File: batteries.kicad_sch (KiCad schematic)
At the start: 29 parts, among them IC1 BQ7791501PWR, Q8 BSZ067N06LS3_G, Q9 BSZ067N06LS3_G

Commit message: Test commit
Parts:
- removed D2, D3, D4: CUS10S30, 30V 1A, CUS357H3F, symbol HEDGE2:CUS10S30
- added C76, C88: 1u, symbol Device:C_Small
- added C77, C78: 10u, symbol Device:C_Small
- added C79, C80, C81, C82, C83, C84, C85, C86, C87: 100n, symbol Device:C_Small
- added D15, D16, D2, D3, D5: CDBA240LL-HF, 40V 2A, DIOM5225X250N, symbol HEDGE2:CDBA240LL-HF
- added D17, D18, D19: LED, symbol Device:LED
- added IC23: BQ24610RGER, QFN50P400X400X100-25N-D, symbol HEDGE2:BQ24610RGER
- added L2: ETQP4M6R8KVK - 6u8, ETQ-P4M_KVK, symbol HEDGE2:ETQP4M6R8KVK
- added Q1, Q3: SI7617DN-T1-GE3, SIS862DNT1GE3, symbol HEDGE2:SI7617DN-T1-GE3
- added R55: 10, symbol Device:R_Small
- added R56: 1k, symbol Device:R_Small
- added R57, R58: 1M, symbol Device:R_Small
- added R59, R60, R61: 100k, symbol Device:R_Small
- added R62: 32k4, symbol Device:R_Small
- added R63, R64, R65, R66: 10k, symbol Device:R_Small
- added R67: 9k31, symbol Device:R_Small
- added R68: 430k, symbol Device:R_Small
- added RSR1: 10m, symbol Device:R_Small
- added TH2: 10k, symbol Device:Thermistor_US
- IC1: value BQ7791501PWR -> BQ7791514PWR
- R7: value 1m -> 10m
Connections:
- net +BATT: now also C76.2, C77.2, C78.2, C80.1, C81.2, C82.2, C83.2, C84.1, C84.2, C85.1, C85.2, C86.1, C87.2, C88.2, IC23.13 (SRN), IC23.17 (GND), IC23.25 (EP), Q1.1 (S_1), Q1.2 (S_2), Q1.3 (S_3), R57.2, R58.1, R62.1, R63.1, R68.1, RSR1.2, TH2.1
- net at Q9.1 (S_1), Q9.2 (S_2), Q9.3 (S_3)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: now also D3.2 (A)
- net at R10.1, R11.2: now also D2.2 (A)
- net at IC1.11 (SRN), Q8.1 (S_1), Q8.2 (S_2)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: now also D5.2 (A)
- net at Q8.5 (D_1), Q8.6 (D_2), Q8.7 (D_3)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: now also D3.1 (K), D5.1 (K)
- net at Q9.4 (G), R11.1, R12.2: now also D2.1 (K)
- new net: IC23.11 (ISET1), R61.1, R63.2
- new net: C77.1, C78.1, D16.1 (K), IC23.1 (ACN), IC23.2 (ACP), Q3.5 (D_1), Q3.6 (D_2), Q3.7 (D_3), Q3.8 (D_4), R55.2
- new net: D19.2 (A), R66.2
- new net: C76.1, IC23.24 (VCC), R55.1
- new net: IC23.15 (ISET2), R60.1, R62.2
- new net: C79.2, IC23.20 (PH), L2.1, Q1.5 (D_1), Q1.6 (D_2), Q1.7 (D_3), Q1.8 (D_4), Q3.1 (S_1), Q3.2 (S_2), Q3.3 (S_3)
- new net: IC23.21 (HIDRV), Q3.4 (G)
- new net: D17.2 (A), R64.2
- new net: C80.2, D15.2 (A), IC23.18 (REGN)
- new net: IC23.19 (LODRV), Q1.4 (G)
- new net: D15.1 (K), IC23.22 (BTST), R56.1
- new net: D17.1 (K), IC23.5 (STAT1)
- new net: IC23.6 (TS), R67.1, R68.2, TH2.2
- new net: C81.1, IC23.7 (TTC)
- new net: D19.1 (K), IC23.8 (~{PG})
- new net: D18.1 (K), IC23.9 (STAT2)
- new net: D18.2 (A), R65.2
- new net: C79.1, R56.2
- new net: C87.1, R59.1
- new net +ADAPTER: D16.2 (A), R59.2
- new net SRP: C82.1, C83.1, IC23.14 (SRP), L2.2, RSR1.1
- new net VFB: C86.2, IC23.12 (VFB), R57.1, R58.2
- new net VREF: C88.1, IC23.10 (VREF), IC23.16 (ACSET), IC23.4 (CE), R60.2, R61.2, R64.1, R65.1, R66.1, R67.2
- no-connect marks 4 -> 6
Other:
- note added: "Adjust R_SNS to set the over-current trip point."
- moved on the sheet: BT1, C2, C3, C4, C5, C6, C7, IC1, Q8, Q9, R1, R10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

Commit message: updated battery sheet passives values
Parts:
- C80: value 100n -> 1u
- C81: value 100n -> 56n
- C84, C85: value 100n -> 10u
- C86: value 100n -> 22p
- R56: value 1k -> 10
- R57: value 1M -> 500k
- R58: value 1M -> 100k
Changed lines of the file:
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@@
 			)
 		)
-		(property "Value" "1M"
-			(at 202.184 143.256 0)
+		(property "Value" "500k"
+			(at 202.438 143.256 0)
 			(effects
 				(font
@@
 			)
 		)
-		(property "Value" "100n"
+		(property "Value" "10u"
 			(at 215.392 137.922 0)
 			(effects
@@
 			)
 		)
-		(property "Value" "100n"
-			(at 107.188 135.636 0)
+		(property "Value" "1u"
+			(at 104.902 135.636 0)
 			(effects
 				(font
@@
 			)
 		)
-		(property "Value" "1M"
-			(at 202.184 150.876 0)
+		(property "Value" "100k"
+			(at 202.692 150.876 0)
 			(effects
 				(font
@@
 			)
 		)
-		(property "Value" "100n"
+		(property "Value" "56n"
 			(at 99.314 148.336 90)
 			(effects
@@
 			)
 		)
-		(property "Value" "1k"
+		(property "Value" "10"
 			(at 122.174 134.366 90)
 			(effects
@@
 			)
 		)
-		(property "Value" "100n"
+		(property "Value" "10u"
 			(at 225.552 137.922 0)
 			(effects
@@
 			)
 		)
-		(property "Value" "100n"
+		(property "Value" "22p"
 			(at 209.042 142.748 0)
 			(effects

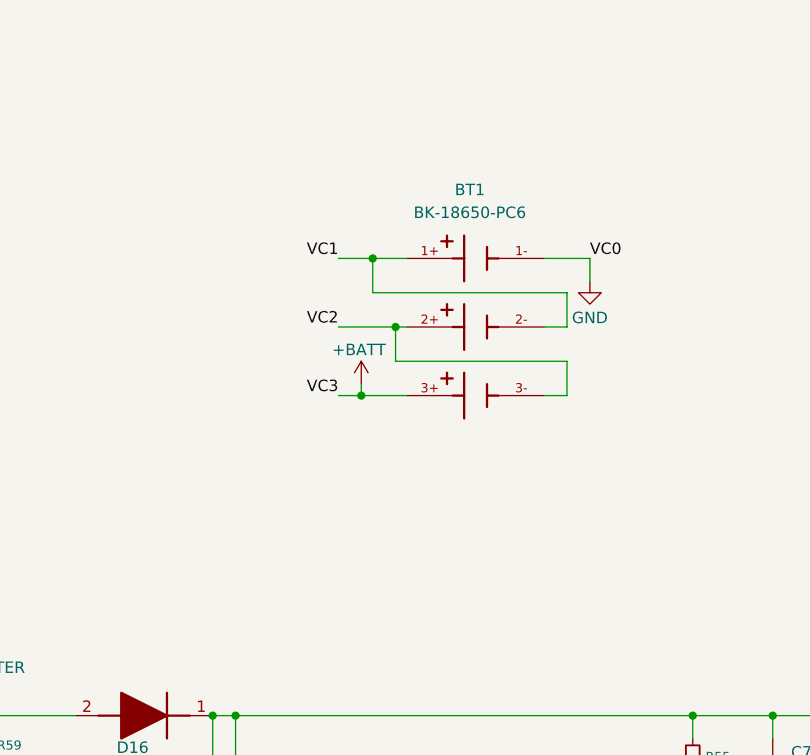
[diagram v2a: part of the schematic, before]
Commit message: updates to connectors
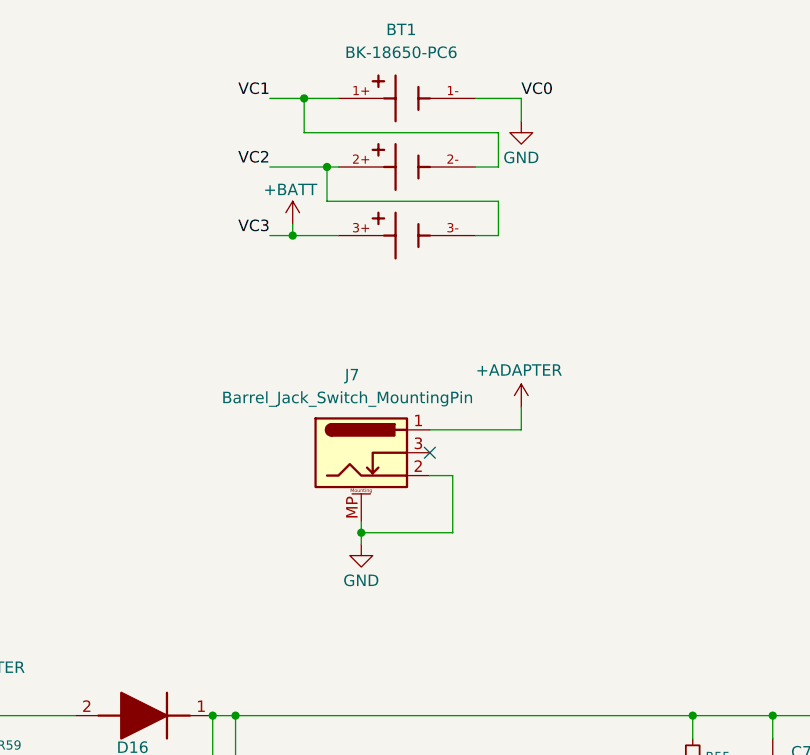
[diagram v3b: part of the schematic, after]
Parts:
- added J7: Barrel_Jack_Switch_MountingPin, symbol Connector:Barrel_Jack_Switch_MountingPin
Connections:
- net +ADAPTER: now also J7.1
- net +BATT: now also J7.2, J7.MP (MountPin)
- no-connect marks 6 -> 7
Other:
- moved on the sheet: BT1

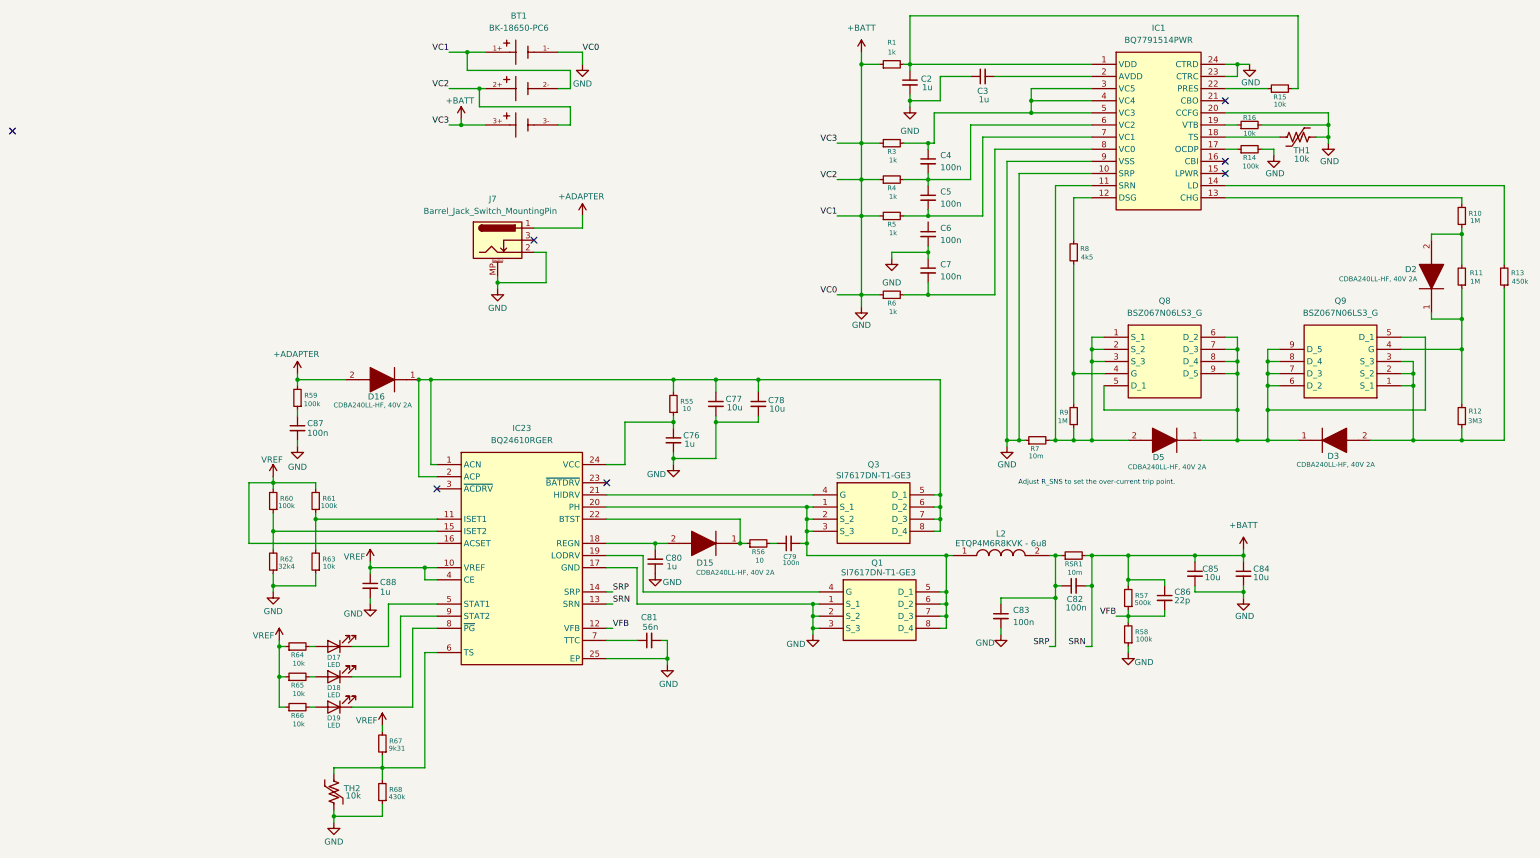
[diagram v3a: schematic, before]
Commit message: updated the schematic to remove connection to rocksat, linked schmatic symbols to footprints
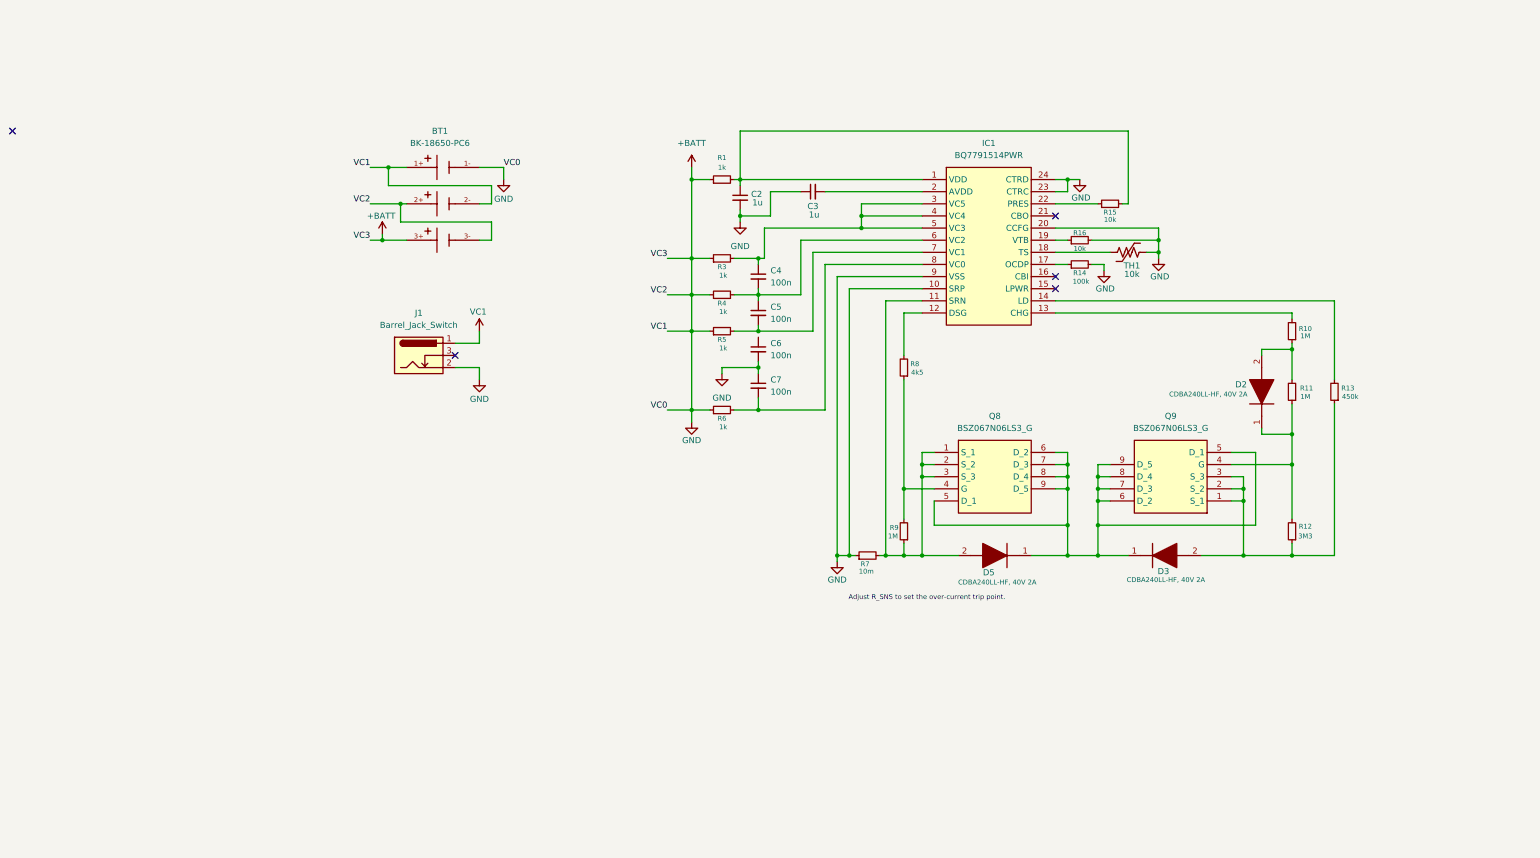
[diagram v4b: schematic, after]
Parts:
- removed C76, C80, C88: 1u, symbol Device:C_Small
- removed C77, C78, C84, C85: 10u, symbol Device:C_Small
- removed C79, C82, C83, C87: 100n, symbol Device:C_Small
- removed C81: 56n, symbol Device:C_Small
- removed C86: 22p, symbol Device:C_Small
- removed D15, D16: CDBA240LL-HF, 40V 2A, DIOM5225X250N, symbol HEDGE2:CDBA240LL-HF
- removed D17, D18, D19: LED, symbol Device:LED
- removed IC23: BQ24610RGER, QFN50P400X400X100-25N-D, symbol HEDGE2:BQ24610RGER
- removed J7: Barrel_Jack_Switch_MountingPin, symbol Connector:Barrel_Jack_Switch_MountingPin
- removed L2: ETQP4M6R8KVK - 6u8, ETQ-P4M_KVK, symbol HEDGE2:ETQP4M6R8KVK
- removed Q1, Q3: SI7617DN-T1-GE3, SIS862DNT1GE3, symbol HEDGE2:SI7617DN-T1-GE3
- removed R55, R56: 10, symbol Device:R_Small
- removed R57: 500k, symbol Device:R_Small
- removed R58, R59, R60, R61: 100k, symbol Device:R_Small
- removed R62: 32k4, symbol Device:R_Small
- removed R63, R64, R65, R66: 10k, symbol Device:R_Small
- removed R67: 9k31, symbol Device:R_Small
- removed R68: 430k, symbol Device:R_Small
- removed RSR1: 10m, symbol Device:R_Small
- removed TH2: 10k, symbol Device:Thermistor_US
- added J1: Barrel_Jack_Switch, Connector_BarrelJack:BarrelJack_CUI_PJ-102AH_Horizontal, symbol Connector:Barrel_Jack_Switch
- BT1: footprint BK-18650-PC6:BAT_BK-18650-PC6 -> HEDGE2:BK18650PC6
- C2, C3: footprint (none) -> Capacitor_SMD:C_0603_1608Metric
- C4, C5, C6, C7: footprint (none) -> Capacitor_SMD:C_0402_1005Metric
- D2, D3, D5: footprint DIOM5225X250N -> HEDGE2:CDBA240LL-HF
- IC1: footprint SOP65P640X120-24N -> HEDGE2:BQ7791501PWR
- Q8, Q9: footprint BSZ067N06LS3G -> HEDGE2:BSZ067N06LS3G
- R1, R10, R11, R12, R13, R14, R15, R16, R3, R4, R5, R6, R7, R8, R9, TH1: footprint (none) -> Resistor_SMD:R_0402_1005Metric
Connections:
- net +BATT: now also J1.1, J1.2
- no-connect marks 7 -> 5
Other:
- moved on the sheet: BT1, C2, C3, C4, C5, C6, C7, D2, D3, D5, IC1, Q8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

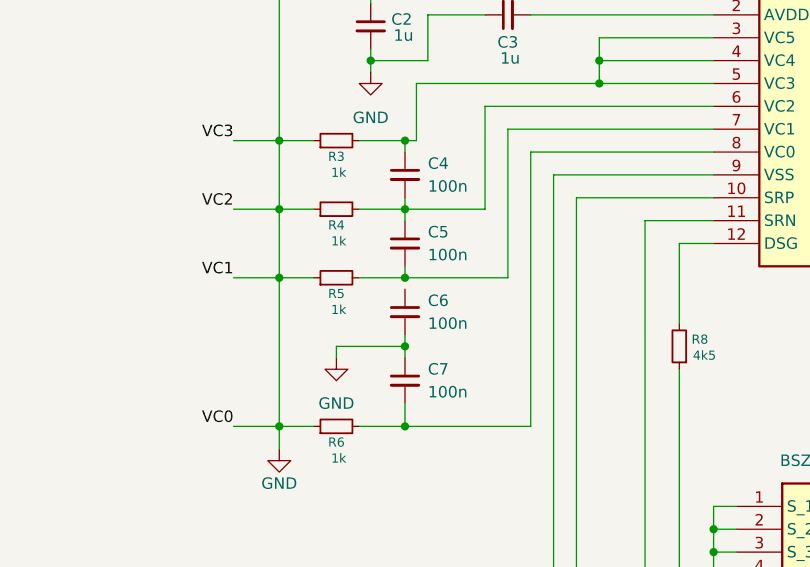
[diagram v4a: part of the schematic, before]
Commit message: Added most 3d models, continued layout
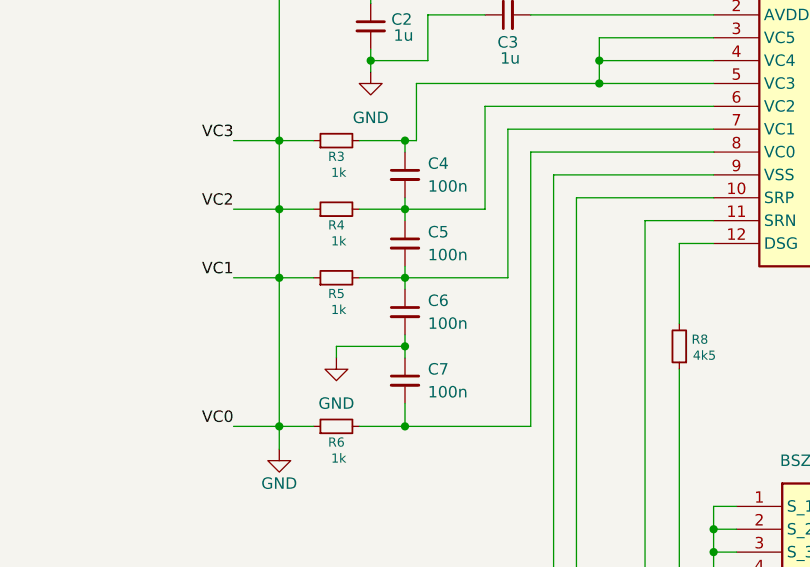
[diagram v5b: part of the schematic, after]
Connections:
- net at C6.1: now also C5.2, IC1.7 (VC1), R5.2
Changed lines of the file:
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@@
+	(wire
+		(pts
+			(xy 121.92 86.36) (xy 121.92 87.63)
+		)
+		(stroke
+			(width 0)
+			(type default)
+		)
+	)
 	(wire
 		(pts

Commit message: Initial layout completed
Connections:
- net +BATT: no longer BT1.1+, BT1.1-, BT1.2+, BT1.2-, BT1.3-, C2.2, C3.1, C6.2, C7.1, IC1.10 (SRP), IC1.20 (CCFG), IC1.23 (CTRC), IC1.24 (CTRD), IC1.9 (VSS), J1.2, R14.2, R16.2, R4.1, R5.1, R6.1, R7.1, TH1.2
- net PACK-: now reaches D3.2 (A), Q9.1 (S_1), Q9.2 (S_2), Q9.3 (S_3), R12.1, R13.1
- net PACK-: now also J1.2
- new net GND: BT1.1-, C2.2, C3.1, C6.2, C7.1, IC1.10 (SRP), IC1.20 (CCFG), IC1.23 (CTRC), IC1.24 (CTRD), IC1.9 (VSS), R14.2, R16.2, R6.1, R7.1, TH1.2
- new net VC1: BT1.1+, BT1.2-, R5.1
- new net VC2: BT1.2+, BT1.3-, R4.1
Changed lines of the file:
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@@
 	)
 	(junction
+		(at 242.57 133.35)
+		(diameter 0)
+		(color 0 0 0 0)
+	)
+	(junction
 		(at 44.45 52.07)
 		(diameter 0)
@@
 	)
 	(junction
-		(at 107.95 71.12)
-		(diameter 0)
-		(color 0 0 0 0)
-	)
-	(junction
 		(at 205.74 69.85)
 		(diameter 0)
@@
 	)
 	(junction
-		(at 107.95 86.36)
-		(diameter 0)
-		(color 0 0 0 0)
-	)
-	(junction
 		(at 186.69 114.3)
 		(diameter 0)
@@
 	)
 	(junction
-		(at 107.95 78.74)
-		(diameter 0)
-		(color 0 0 0 0)
-	)
-	(junction
 		(at 223.52 133.35)
 		(diameter 0)
@@
 	)
 	(junction
-		(at 107.95 54.61)
-		(diameter 0)
-		(color 0 0 0 0)
-	)
-	(junction
 		(at 193.04 119.38)
 		(diameter 0)
@@
 	(wire
 		(pts
-			(xy 107.95 78.74) (xy 107.95 86.36)
-		)
-		(stroke
-			(width 0)
-			(type default)
-		)
-	)
-	(wire
-		(pts
 			(xy 184.15 116.84) (xy 186.69 116.84)
 		)
@@
 	(wire
 		(pts
-			(xy 107.95 71.12) (xy 107.95 54.61)
-		)
-		(stroke
-			(width 0)
-			(type default)
-		)
-	)
-	(wire
-		(pts
 			(xy 184.15 64.77) (xy 205.74 64.77)
 		)
@@
 	(wire
 		(pts
-			(xy 102.87 86.36) (xy 107.95 86.36)
+			(xy 102.87 86.36) (xy 111.76 86.36)
 		)
 		(stroke
@@
 	(wire
 		(pts
+			(xy 242.57 133.35) (xy 242.57 134.62)
+		)
+		(stroke
+			(width 0)
+			(type default)
+		)
+	)
+	(wire
+		(pts
 			(xy 118.11 54.61) (xy 118.11 55.88)
 		)
@@
 	(wire
 		(pts
-			(xy 107.95 71.12) (xy 102.87 71.12)
+			(xy 102.87 71.12) (xy 111.76 71.12)
 		)
 		(stroke
@@
 	(wire
 		(pts
-			(xy 111.76 71.12) (xy 107.95 71.12)
-		)
-		(stroke
-			(width 0)
-			(type default)
-		)
-	)
-	(wire
-		(pts
 			(xy 186.69 111.76) (xy 186.69 114.3)
 		)
@@
 	(wire
 		(pts
-			(xy 107.95 78.74) (xy 111.76 78.74)
-		)
-		(stroke
-			(width 0)
-			(type default)
-		)
-	)
-	(wire
-		(pts
 			(xy 152.4 82.55) (xy 152.4 91.44)
 		)
@@
 	(wire
 		(pts
-			(xy 107.95 71.12) (xy 107.95 78.74)
-		)
-		(stroke
-			(width 0)
-			(type default)
-		)
-	)
-	(wire
-		(pts
 			(xy 184.15 59.69) (xy 193.04 59.69)
 		)
@@
 	(wire
 		(pts
-			(xy 107.95 86.36) (xy 107.95 102.87)
-		)
-		(stroke
-			(width 0)
-			(type default)
-		)
-	)
-	(wire
-		(pts
 			(xy 156.21 80.01) (xy 148.59 80.01)
 		)
@@
 	(wire
 		(pts
-			(xy 107.95 78.74) (xy 102.87 78.74)
+			(xy 102.87 78.74) (xy 111.76 78.74)
 		)
 		(stroke
@@
 	(wire
 		(pts
-			(xy 107.95 86.36) (xy 111.76 86.36)
-		)
-		(stroke
-			(width 0)
-			(type default)
-		)
-	)
-	(wire
-		(pts
 			(xy 233.68 82.55) (xy 233.68 83.82)
 		)
@@
 			)
 		)
-		(property "Value" "GND"
+		(property "Value" "PACK-"
 			(at 63.5 100.584 0)
 			(effects
@@
 	)
 	(symbol
+		(lib_id "power:GND")
+		(at 242.57 134.62 0)
+		(unit 1)
+		(exclude_from_sim no)
+		(in_bom yes)
+		(on_board yes)
+		(dnp no)
+		(property "Reference" "#PWR013"
+			(at 242.57 140.97 0)
+			(effects
+				(font
+					(size 1.27 1.27)
+				)
+				(hide yes)
+			)
+		)
+		(property "Value" "PACK-"
+			(at 242.57 138.684 0)
+			(effects
+				(font
+					(size 1.27 1.27)
+				)
+			)
+		)
+		(property "Footprint" ""
+			(at 242.57 134.62 0)
+			(effects
+				(font
+					(size 1.27 1.27)
+				)
+				(hide yes)
+			)
+		)
+		(property "Datasheet" ""
+			(at 242.57 134.62 0)
+			(effects
+				(font
+					(size 1.27 1.27)
+				)
+				(hide yes)
+			)
+		)
+		(property "Description" "Power symbol creates a global label with name \"GND\" , ground"
+			(at 242.57 134.62 0)
+			(effects
+				(font
+					(size 1.27 1.27)
+				)
+				(hide yes)
+			)
+		)
+		(pin "1"
+		)
+		(instances
+			(project "EPS"
+				(path "/7b605902-d0e0-4baa-b797-611cfe27637f/66850c0b-0984-482d-8867-bea587885772"
+					(reference "#PWR013")
+					(unit 1)
+				)
+			)
+		)
+	)
+	(symbol
 		(lib_id "Device:R_Small")
 		(at 114.3 86.36 90)
@@
 			)
 		)
-		(property "Value" "VC1"
+		(property "Value" "+BATT"
 			(at 63.246 82.296 0)
 			(effects
@@
 		(on_board yes)
 		(dnp no)
-		(fields_autoplaced yes)
 		(property "Reference" "#PWR02"
 			(at 114.3 101.6 0)
@@
 		)
 		(property "Value" "GND"
-			(at 114.3 100.33 0)
+			(at 114.554 99.568 0)
 			(effects
 				(font
